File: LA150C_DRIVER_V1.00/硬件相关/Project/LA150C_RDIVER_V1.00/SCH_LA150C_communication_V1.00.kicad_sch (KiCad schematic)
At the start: 4 parts, among them U3 TCAN3413DDFR

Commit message: chore: save LA150C schematic updates
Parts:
- removed R11: 120R(DNP), symbol Device:R
- renumbered C13 to C33, U3 to U5
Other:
- moved on the sheet: C33, D2

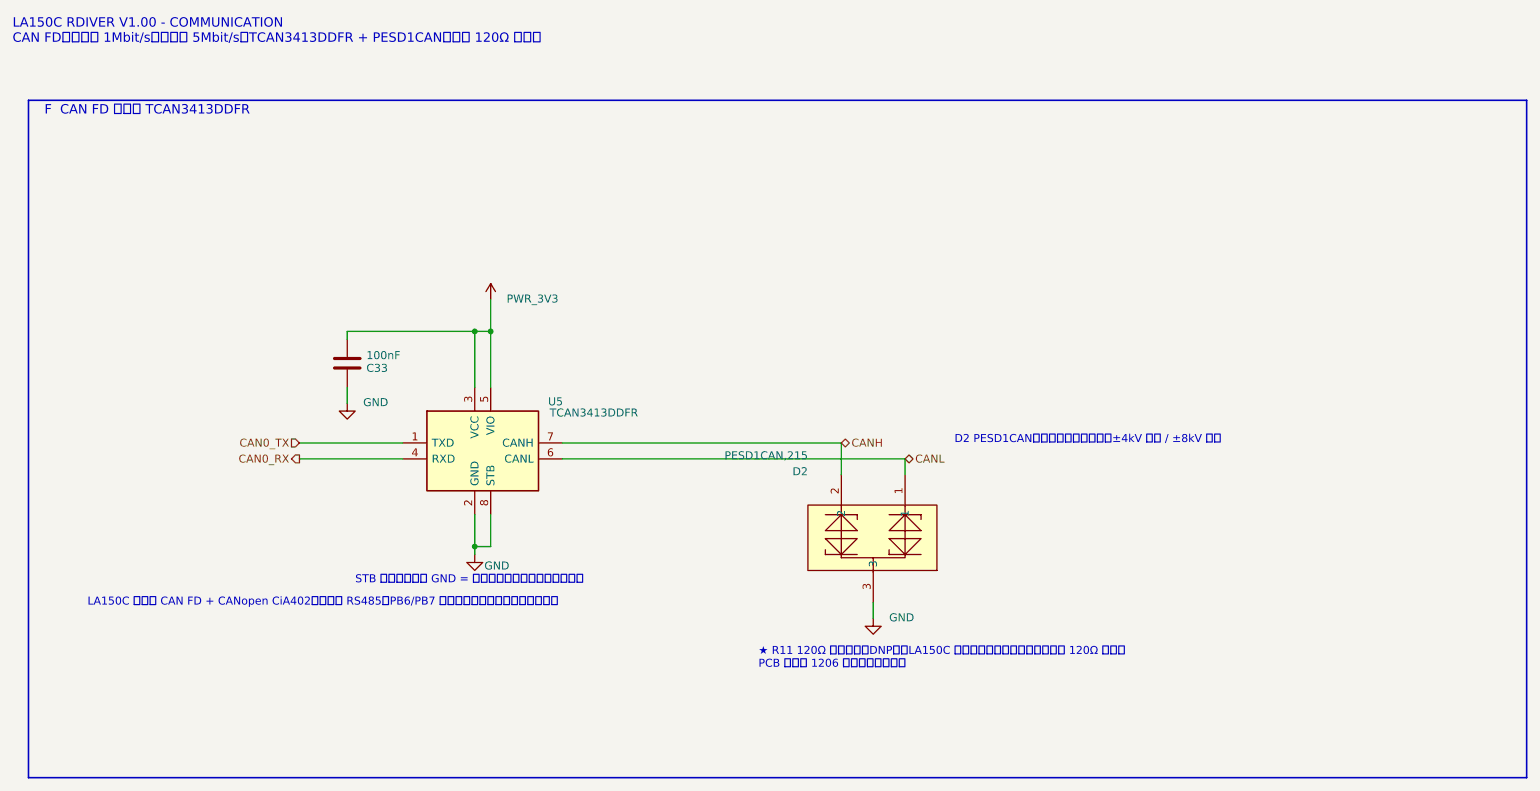
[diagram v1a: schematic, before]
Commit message: feat: finalize LA150C driver schematic
Align the GD32F503 BGA64 pin resources with QS01 V1.12, retain the SCT2230, MT6701 and CAN FD circuits, replace the motor test points with 1.0 x 2.0 mm solder pads, and update the symbols, footprints, ERC report, netlist, BOM and PDF.
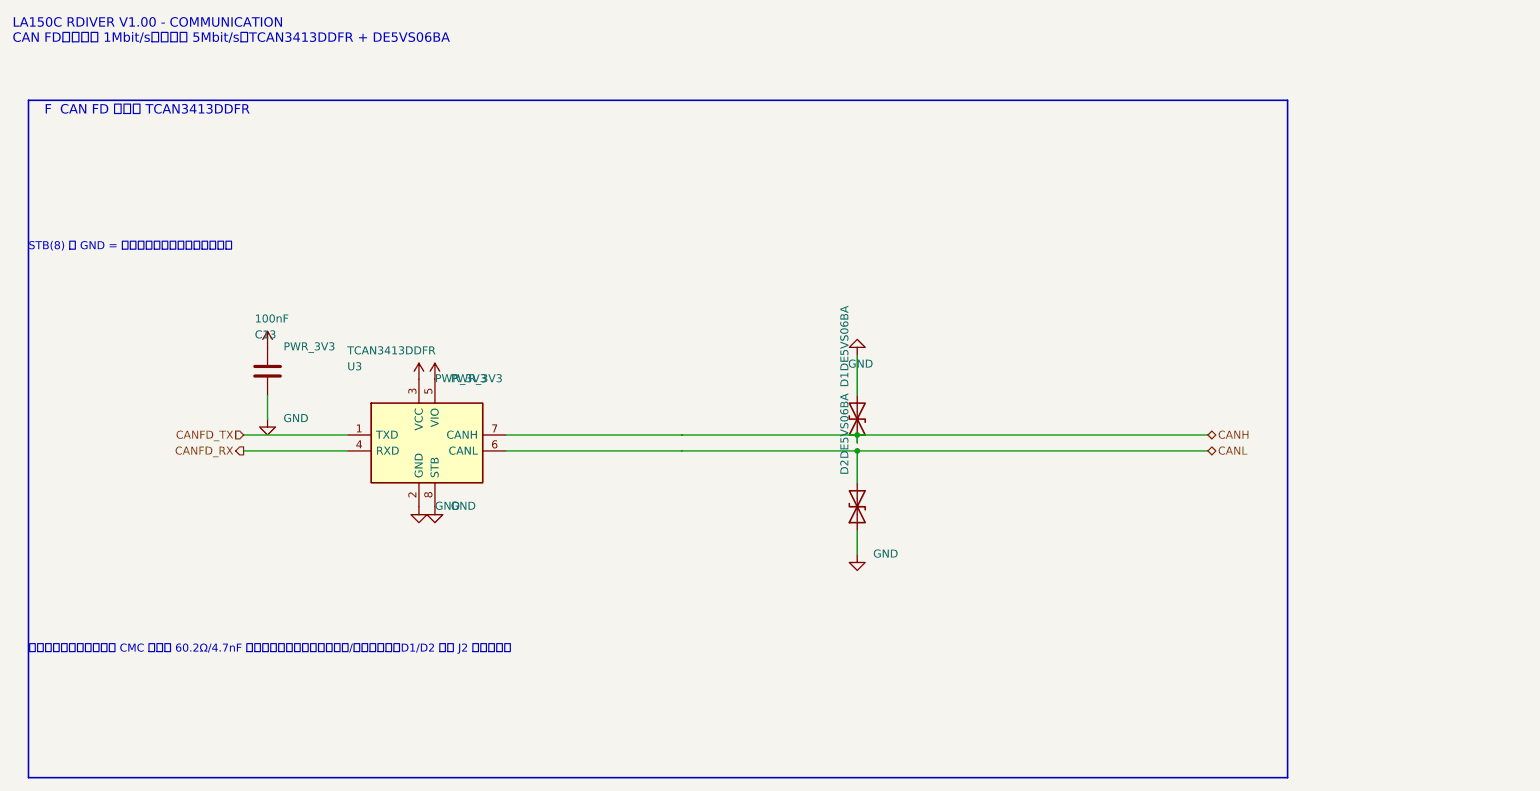
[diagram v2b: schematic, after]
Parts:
- added D1: DE5VS06BA, Circuit Protection:D_0201_0603Metric, symbol LA150C_RDIVER_V1.00:DE5VS06BA
- C13: renamed from C33; footprint Capacitors:C_0402_1005Metric -> Capacitors:C0201; symbol LA150C_RDIVER_V1.00:GRM155R71H104KE14D -> LA150C_RDIVER_V1.00:GRM033Z71C104KE14D; LCSC Part C77020 -> C668346; MPN GRM155R71H104KE14D -> GRM033Z71C104KE14D
- D2: value PESD1CAN,215 -> DE5VS06BA; footprint Transistors:SOT-23_L2.9-W1.3-P1.90-LS2.4-BR -> Circuit Protection:D_0201_0603Metric; symbol LA150C_RDIVER_V1.00:PESD1CAN,215 -> LA150C_RDIVER_V1.00:DE5VS06BA; LCSC Part C15771 -> C9900301658; MPN PESD1CAN,215 -> (none); Manufacturer Nexperia(安世) -> (none)
- renumbered U5 to U3
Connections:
- net CANH: now also D1.1 (A1); no longer D2.2
- net CANL: now also D2.2 (A2); no longer D2.1
- net GND: now also D2.1 (A1), D1.2 (A2); no longer D2.3
- net CAN0_RX renamed CANFD_RX
- net CAN0_TX renamed CANFD_TX
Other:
- note added: "LA150C RDIVER V1.00 - COMMUNICATION CAN FD：仲裁段 1Mbit/s，数据段 5Mbit/s；TCAN3413DDFR + DE5VS06BA"
- note added: "STB(8) 接 GND = 正常工作模式；高电平为待机。"
- note added: "因板空间受限，本版取消 CMC 与板内 60.2Ω/4.7nF 分裂终端；总线段终端由线缆/系统端实现。D1/D2 靠近 J2 接口放置。"
- note removed: "D2 PESD1CAN：连接器侧就近布置，±4kV 接触 / ±8kV 空气"
- note removed: "LA150C RDIVER V1.00 - COMMUNICATION CAN FD：仲裁段 1Mbit/s，数据段 5Mbit/s；TCAN3413DDFR + PESD1CAN；板内 120Ω 不贴片"
- note removed: "LA150C 仅保留 CAN FD + CANopen CiA402，不保留 RS485（PB6/PB7 已改作一维力传感器预留输入）。"
- note removed: "STB 内部上拉；接 GND = 正常工作模式（高电平为待机）"
- note removed: "★ R11 120Ω 默认不贴（DNP）：LA150C 不内置终端，由总线两端各一只 120Ω 承担。 PCB 仅预留 1206 焊盘供调试装配。"
- moved on the sheet: C13, U3
